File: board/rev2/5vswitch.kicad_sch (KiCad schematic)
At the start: 13 parts, among them Q1 WSD40120DN56G, U3 LM5050-1, U4 TPS259472ARPWR

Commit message: Board GPIO allocation
- and usbmux

still need to do termination on the big buses + a bunch of bypass caps
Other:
- company: (none) -> MLABS
- title: (none) -> 5V Multiplexer
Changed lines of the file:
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@@
 	(generator_version "9.0")
 	(paper "A4")
+	(title_block
+		(title "5V Multiplexer")
+		(rev "A")
+		(company "MLABS")
+		(comment 1 "MSign-NG")
+	)
 	(junction
 		(at 220.98 71.12)

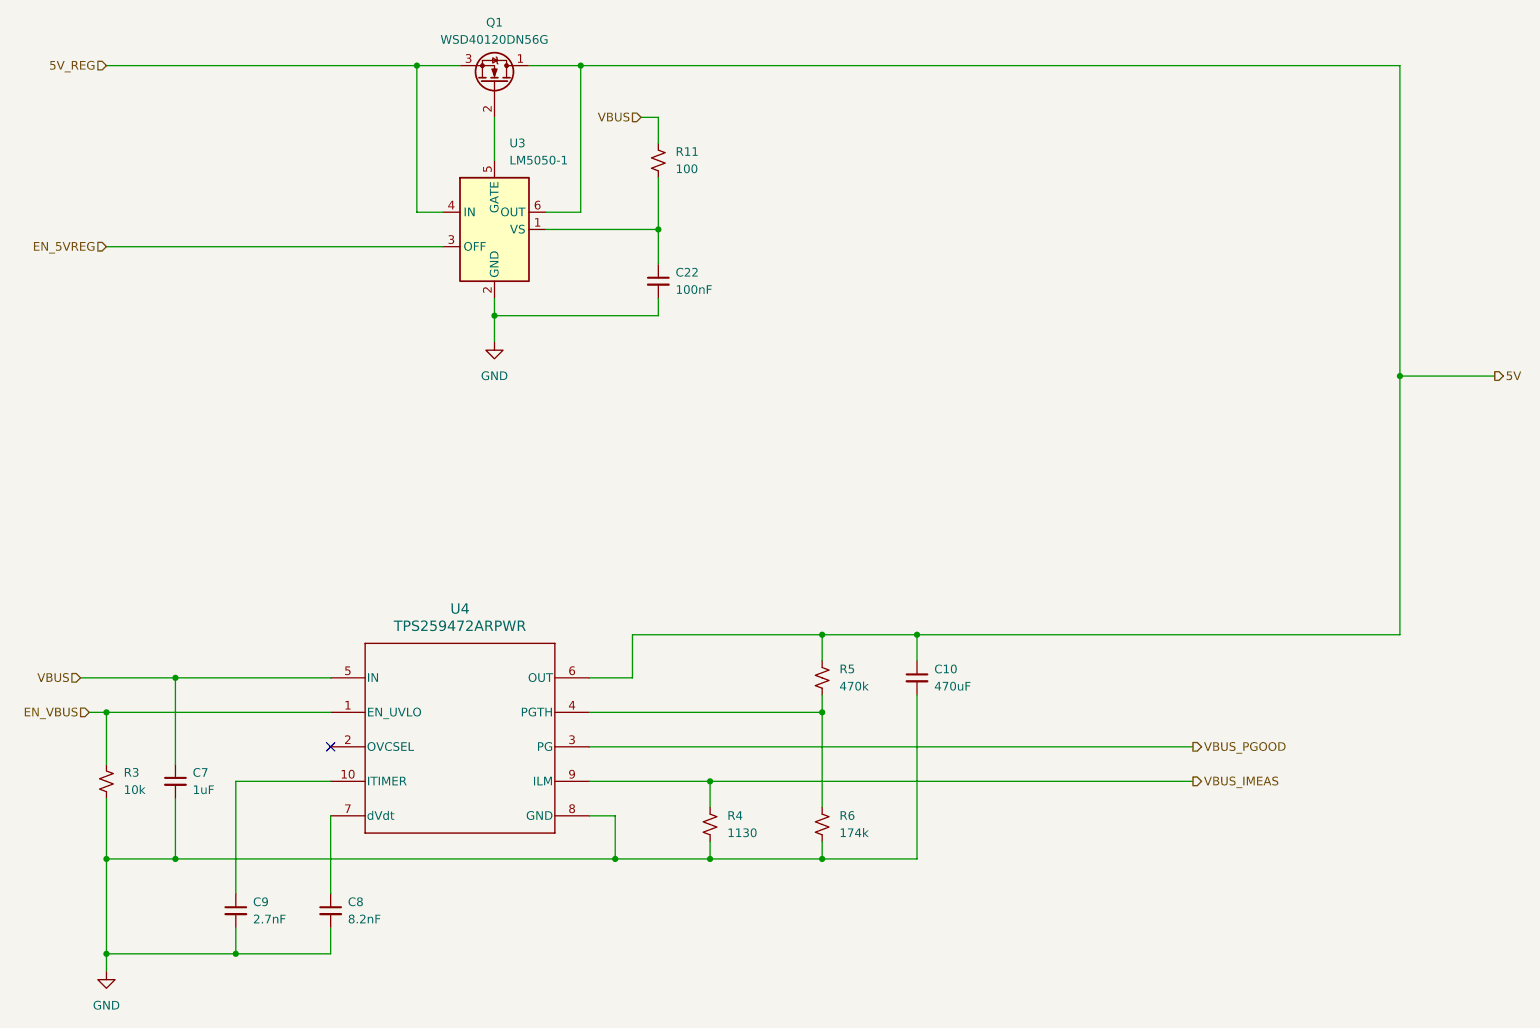
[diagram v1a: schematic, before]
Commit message: Continue board, assign caps/res, adjust for JLC availability
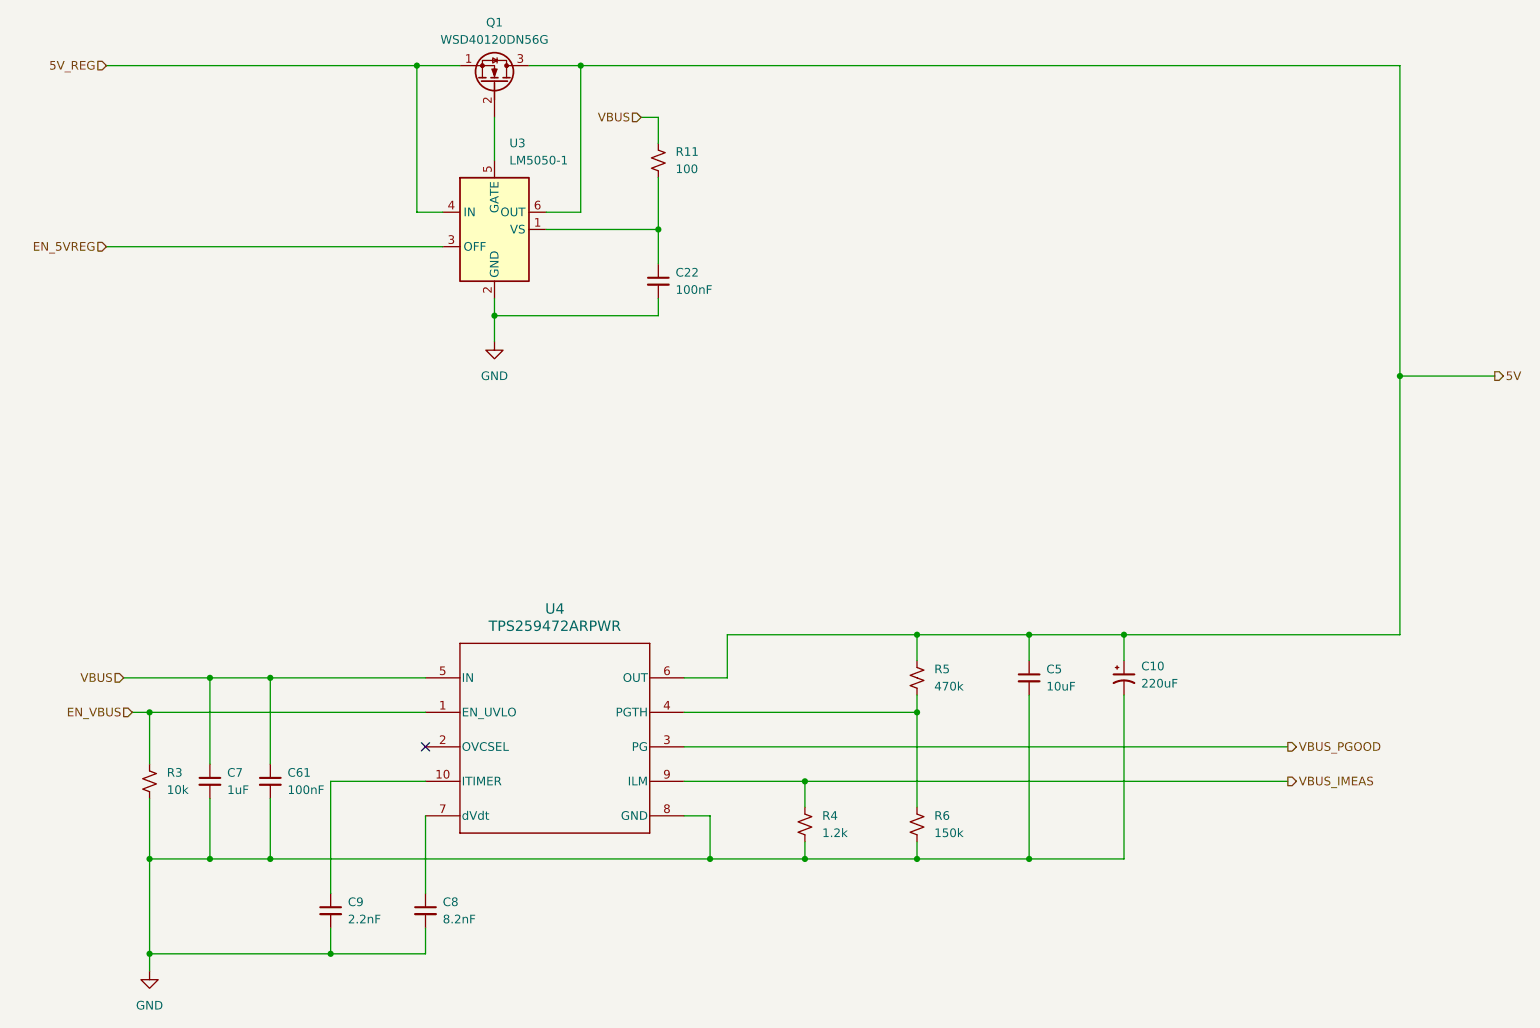
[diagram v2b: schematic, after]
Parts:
- added C5: 10uF, Capacitor_SMD:C_1210_3225Metric, symbol Device:C_Small
- added C61: 100nF, Capacitor_SMD:C_0402_1005Metric, symbol Device:C_Small
- C10: value 470uF -> 220uF; footprint (none) -> Capacitor_THT:CP_Radial_D8.0mm_P3.50mm; symbol Device:C_Small -> Device:C_Polarized_Small_US; Part (none) -> ERS1VM221F12OT
- C22: footprint (none) -> Capacitor_SMD:C_0402_1005Metric; Part (none) -> CL05B104KB54PNC
- C7: footprint (none) -> Capacitor_SMD:C_0603_1608Metric; Part (none) -> CL10A105KB8NNNC
- C8: footprint (none) -> Capacitor_SMD:C_0603_1608Metric; Part (none) -> 0603B822K500NT
- C9: value 2.7nF -> 2.2nF; footprint (none) -> Capacitor_SMD:C_0603_1608Metric; Part (none) -> 0603B222K500NT
- Q1: footprint (none) -> Transistor_FET_Winsok:DFN-8_L4.9-W6.0-P1.27-LS6.1-BL; symbol Device:Q_NMOS_DGS -> Transistor_FET:Q_NMOS_SGD
- R11: footprint (none) -> Resistor_SMD:R_1206_3216Metric; Part (none) -> 1206W4F1000T5E
- R3: footprint (none) -> Resistor_SMD:R_0805_2012Metric; Part (none) -> 0805W8F1002T5E
- R4: value 1130 -> 1.2k; footprint (none) -> Resistor_SMD:R_0805_2012Metric; Part (none) -> 0805W8F1201T5E
- R5: footprint (none) -> Resistor_SMD:R_0805_2012Metric; Part (none) -> 0805W8F4703T5E
- R6: value 174k -> 150k; footprint (none) -> Resistor_SMD:R_0805_2012Metric; Part (none) -> 0805W8F1503T5E
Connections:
- net 5V: now also Q1.3 (D), C5.1; no longer Q1.1 (D)
- net 5V_REG: now also Q1.1 (S); no longer Q1.3 (S)
- net GND: now also C5.2, C61.2
- net VBUS: now also C61.1
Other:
- moved on the sheet: C7, C8, C9, R3, R4, R5, R6, U4

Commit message: Start new PCB
- all footprints setup
- need to setup netclasses next, tho
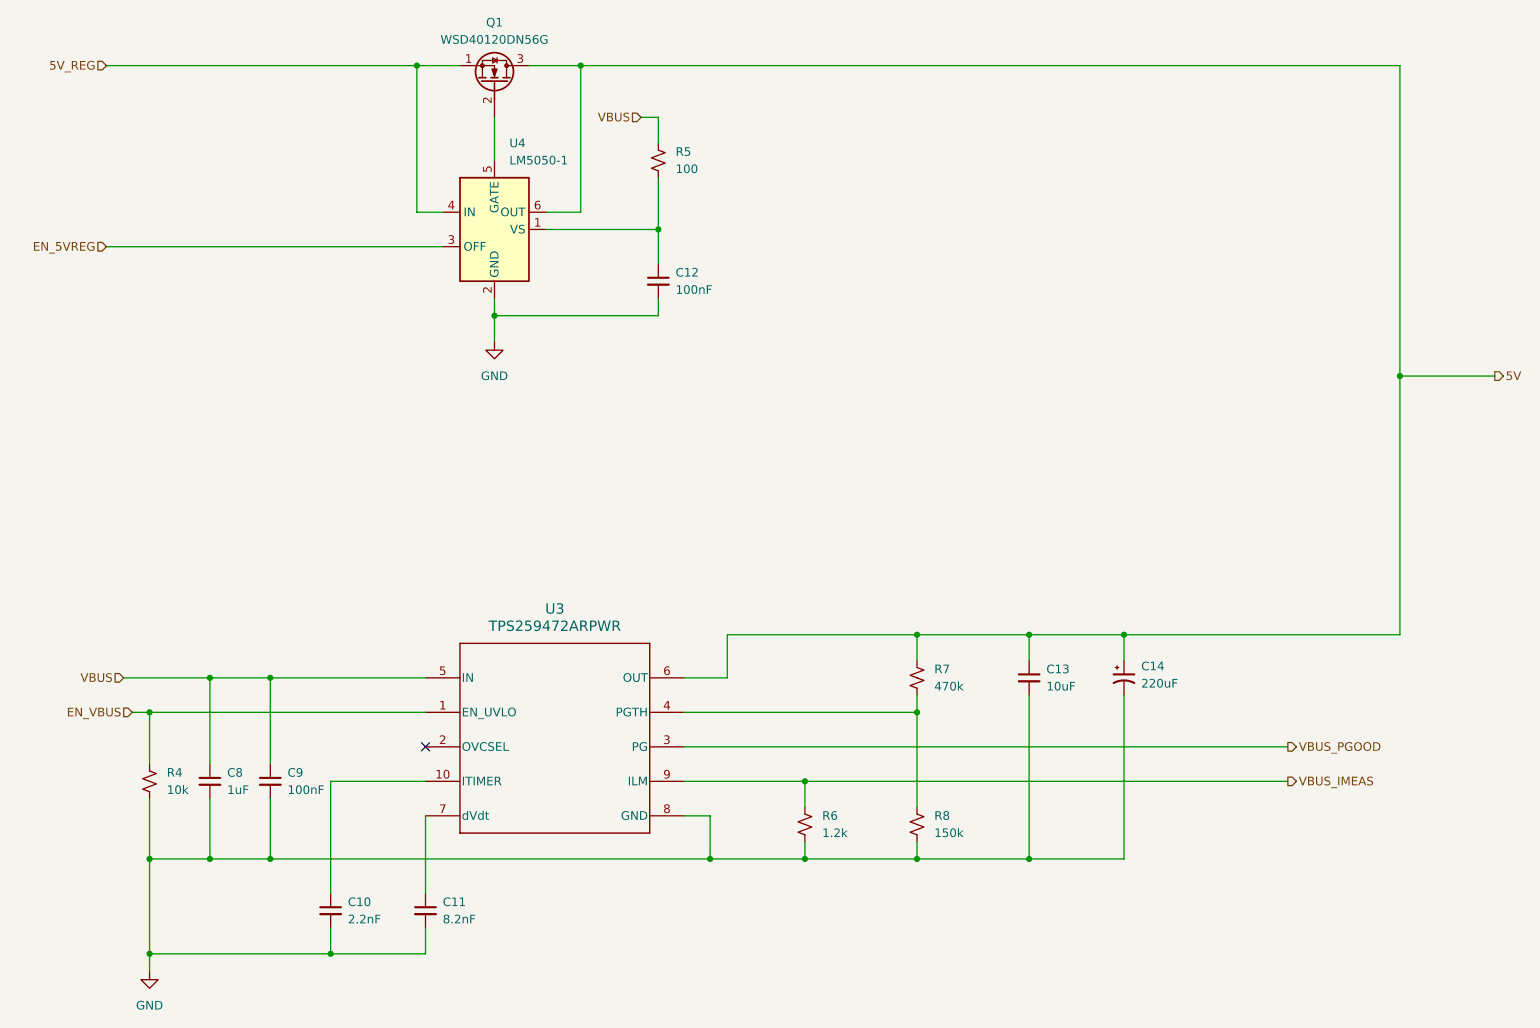
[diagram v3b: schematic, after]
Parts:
- Q1: Part (none) -> WSD40120DN56G
- U3: renamed from U4; footprint RPW0010A-MFG -> TI_EFuse:VQFN-10_L2.0-W2.0-P0.45-TL; Part (none) -> TPS259472ARPWR
- U4: renamed from U3; Part (none) -> LM5050-1
- renumbered C9 to C10, C8 to C11, C22 to C12, C5 to C13, C10 to C14, C7 to C8, C61 to C9, R3 to R4, R11 to R5, R4 to R6, R5 to R7, R6 to R8
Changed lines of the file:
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@@
 		(dnp no)
 		(fields_autoplaced yes)
-		(property "Reference" "C10"
+		(property "Reference" "C14"
 			(at 182.88 113.8681 0)
 			(effects
@@
 			(project "mainboard"
 				(path "/32eb05c7-b4a6-42f3-8fb3-43453631100f/802d77e5-f72d-443e-abfe-d20b44acef6c/65e76cbc-a8ae-47e0-859c-8ff07b1a8d6c"
-					(reference "C10")
+					(reference "C14")
 					(unit 1)
 				)
@@
 		(dnp no)
 		(fields_autoplaced yes)
-		(property "Reference" "C5"
+		(property "Reference" "C13"
 			(at 168.91 114.3062 0)
 			(effects
@@
 			(project "mainboard"
 				(path "/32eb05c7-b4a6-42f3-8fb3-43453631100f/802d77e5-f72d-443e-abfe-d20b44acef6c/65e76cbc-a8ae-47e0-859c-8ff07b1a8d6c"
-					(reference "C5")
+					(reference "C13")
 					(unit 1)
 				)
@@
 		(dnp no)
 		(fields_autoplaced yes)
-		(property "Reference" "C22"
+		(property "Reference" "C12"
 			(at 114.3 55.8862 0)
 			(effects
@@
 			(project ""
 				(path "/32eb05c7-b4a6-42f3-8fb3-43453631100f/802d77e5-f72d-443e-abfe-d20b44acef6c/65e76cbc-a8ae-47e0-859c-8ff07b1a8d6c"
-					(reference "C22")
+					(reference "C12")
 					(unit 1)
 				)
@@
 		(dnp no)
 		(fields_autoplaced yes)
-		(property "Reference" "U3"
+		(property "Reference" "U4"
 			(at 89.8241 36.83 0)
 			(effects
@@
 			)
 		)
+		(property "Part" "LM5050-1"
+			(at 87.63 49.53 0)
+			(effects
+				(font
+					(size 1.27 1.27)
+				)
+				(hide yes)
+			)
+		)
 		(pin "6"
 		)
@@
 			(project ""
 				(path "/32eb05c7-b4a6-42f3-8fb3-43453631100f/802d77e5-f72d-443e-abfe-d20b44acef6c/65e76cbc-a8ae-47e0-859c-8ff07b1a8d6c"
-					(reference "U3")
+					(reference "U4")
 					(unit 1)
 				)
@@
 		(dnp no)
 		(fields_autoplaced yes)
-		(property "Reference" "#PWR17"
+		(property "Reference" "#PWR08"
 			(at 87.63 72.39 0)
 			(effects
@@
 			(project ""
 				(path "/32eb05c7-b4a6-42f3-8fb3-43453631100f/802d77e5-f72d-443e-abfe-d20b44acef6c/65e76cbc-a8ae-47e0-859c-8ff07b1a8d6c"
-					(reference "#PWR17")
+					(reference "#PWR08")
 					(unit 1)
 				)
@@
 		(dnp no)
 		(fields_autoplaced yes)
-		(property "Reference" "R4"
+		(property "Reference" "R6"
 			(at 135.89 135.8899 0)
 			(effects
@@
 			(project "mainboard"
 				(path "/32eb05c7-b4a6-42f3-8fb3-43453631100f/802d77e5-f72d-443e-abfe-d20b44acef6c/65e76cbc-a8ae-47e0-859c-8ff07b1a8d6c"
-					(reference "R4")
+					(reference "R6")
 					(unit 1)
 				)
@@
 		(dnp no)
 		(fields_autoplaced yes)
-		(property "Reference" "R3"
+		(property "Reference" "R4"
 			(at 39.37 129.5399 0)
 			(effects
@@
 			(project "mainboard"
 				(path "/32eb05c7-b4a6-42f3-8fb3-43453631100f/802d77e5-f72d-443e-abfe-d20b44acef6c/65e76cbc-a8ae-47e0-859c-8ff07b1a8d6c"
-					(reference "R3")
+					(reference "R4")
 					(unit 1)
 				)
@@
 		(dnp no)
 		(fields_autoplaced yes)
-		(property "Reference" "#PWR09"
+		(property "Reference" "#PWR07"
 			(at 36.83 165.1 0)
 			(effects
@@
 			(project "mainboard"
 				(path "/32eb05c7-b4a6-42f3-8fb3-43453631100f/802d77e5-f72d-443e-abfe-d20b44acef6c/65e76cbc-a8ae-47e0-859c-8ff07b1a8d6c"
-					(reference "#PWR09")
+					(reference "#PWR07")
 					(unit 1)
 				)
@@
 		(dnp no)
 		(fields_autoplaced yes)
-		(property "Reference" "R11"
+		(property "Reference" "R5"
 			(at 114.3 38.0999 0)
 			(effects
@@
 			(project "mainboard"
 				(path "/32eb05c7-b4a6-42f3-8fb3-43453631100f/802d77e5-f72d-443e-abfe-d20b44acef6c/65e76cbc-a8ae-47e0-859c-8ff07b1a8d6c"
-					(reference "R11")
+					(reference "R5")
 					(unit 1)
 				)
@@
 		(dnp no)
 		(fields_autoplaced yes)
-		(property "Reference" "U4"
+		(property "Reference" "U3"
 			(at 96.52 105.41 0)
 			(effects
@@
 			)
 		)
-		(property "Footprint" "RPW0010A-MFG"
+		(property "Footprint" "TI_EFuse:VQFN-10_L2.0-W2.0-P0.45-TL"
 			(at 77.47 115.57 0)
 			(effects
@@
 			)
 		)
+		(property "Part" "TPS259472ARPWR"
+			(at 77.47 115.57 0)
+			(effects
+				(font
+					(size 1.27 1.27)
+				)
+				(hide yes)
+			)
+		)
 		(pin "9"
 		)
@@
 			(project "mainboard"
 				(path "/32eb05c7-b4a6-42f3-8fb3-43453631100f/802d77e5-f72d-443e-abfe-d20b44acef6c/65e76cbc-a8ae-47e0-859c-8ff07b1a8d6c"
-					(reference "U4")
+					(reference "U3")
 					(unit 1)
 				)
@@
 		(dnp no)
 		(fields_autoplaced yes)
-		(property "Reference" "C7"
+		(property "Reference" "C8"
 			(at 48.26 129.5462 0)
 			(effects
@@
 			(project "mainboard"
 				(path "/32eb05c7-b4a6-42f3-8fb3-43453631100f/802d77e5-f72d-443e-abfe-d20b44acef6c/65e76cbc-a8ae-47e0-859c-8ff07b1a8d6c"
-					(reference "C7")
+					(reference "C8")
 					(unit 1)
 				)
@@
 		(dnp no)
 		(fields_autoplaced yes)
-		(property "Reference" "C61"
+		(property "Reference" "C9"
 			(at 57.15 129.5462 0)
 			(effects
@@
 			(project "mainboard"
 				(path "/32eb05c7-b4a6-42f3-8fb3-43453631100f/802d77e5-f72d-443e-abfe-d20b44acef6c/65e76cbc-a8ae-47e0-859c-8ff07b1a8d6c"
-					(reference "C61")
+					(reference "C9")
 					(unit 1)
 				)
@@
 		(dnp no)
 		(fields_autoplaced yes)
-		(property "Reference" "C8"
+		(property "Reference" "C11"
 			(at 80.01 148.5962 0)
 			(effects
@@
 			(project "mainboard"
 				(path "/32eb05c7-b4a6-42f3-8fb3-43453631100f/802d77e5-f72d-443e-abfe-d20b44acef6c/65e76cbc-a8ae-47e0-859c-8ff07b1a8d6c"
-					(reference "C8")
+					(reference "C11")
 					(unit 1)
 				)
@@
 		(dnp no)
 		(fields_autoplaced yes)
-		(property "Reference" "C9"
+		(property "Reference" "C10"
 			(at 66.04 148.5962 0)
 			(effects
@@
 			(project "mainboard"
 				(path "/32eb05c7-b4a6-42f3-8fb3-43453631100f/802d77e5-f72d-443e-abfe-d20b44acef6c/65e76cbc-a8ae-47e0-859c-8ff07b1a8d6c"
-					(reference "C9")
+					(reference "C10")
 					(unit 1)
 				)
@@
 			)
 		)
+		(property "Part" "WSD40120DN56G"
+			(at 87.63 27.94 90)
+			(effects
+				(font
+					(size 1.27 1.27)
+				)
+				(hide yes)
+			)
+		)
 		(pin "1"
 		)
@@
 		(dnp no)
 		(fields_autoplaced yes)
-		(property "Reference" "R6"
+		(property "Reference" "R8"
 			(at 152.4 135.8899 0)
 			(effects
@@
 			(project "mainboard"
 				(path "/32eb05c7-b4a6-42f3-8fb3-43453631100f/802d77e5-f72d-443e-abfe-d20b44acef6c/65e76cbc-a8ae-47e0-859c-8ff07b1a8d6c"
-					(reference "R6")
+					(reference "R8")
 					(unit 1)
 				)
@@
 		(dnp no)
 		(fields_autoplaced yes)
-		(property "Reference" "R5"
+		(property "Reference" "R7"
 			(at 152.4 114.2999 0)
 			(effects
@@
 			(project "mainboard"
 				(path "/32eb05c7-b4a6-42f3-8fb3-43453631100f/802d77e5-f72d-443e-abfe-d20b44acef6c/65e76cbc-a8ae-47e0-859c-8ff07b1a8d6c"
-					(reference "R5")
-					(unit 1)
-				)
+					(reference "R7")
+					(unit 1)
+				)

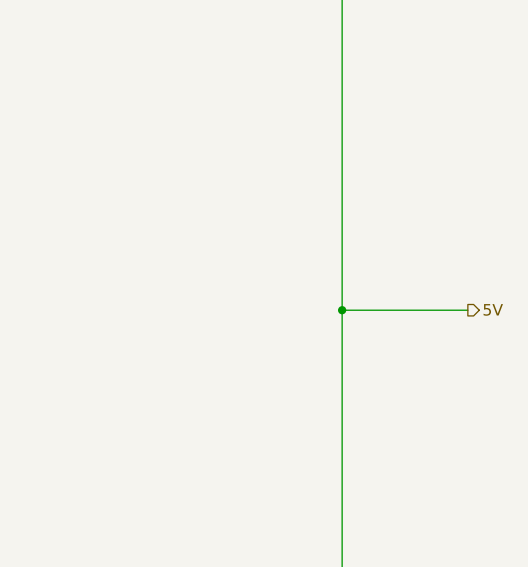
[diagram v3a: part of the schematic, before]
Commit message: Add netclasses, more footprints, fix ERC
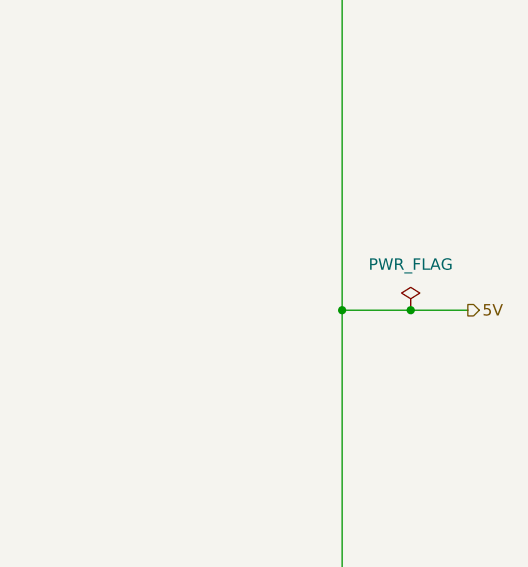
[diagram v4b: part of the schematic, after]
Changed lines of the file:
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@@
+	)
+	(junction
+		(at 228.6 71.12)
+		(diameter 0)
+		(color 0 0 0 0)
 	)
 	(junction
@@
 	(wire
 		(pts
+			(xy 228.6 71.12) (xy 234.95 71.12)
+		)
+		(stroke
+			(width 0)
+			(type default)
+		)
+	)
+	(wire
+		(pts
 			(xy 36.83 120.65) (xy 77.47 120.65)
 		)
@@
 	(wire
 		(pts
-			(xy 220.98 71.12) (xy 234.95 71.12)
+			(xy 220.98 71.12) (xy 228.6 71.12)
 		)
 		(stroke
@@
 					(unit 1)
 				)
+			)
+		)
+	)
+	(symbol
+		(lib_id "power:PWR_FLAG")
+		(at 228.6 71.12 0)
+		(unit 1)
+		(exclude_from_sim no)
+		(in_bom yes)
+		(on_board yes)
+		(dnp no)
+		(fields_autoplaced yes)
+		(property "Reference" "#FLG01"
+			(at 228.6 69.215 0)
+			(effects
+				(font
+					(size 1.27 1.27)
+				)
+				(hide yes)
+			)
+		)
+		(property "Value" "PWR_FLAG"
+			(at 228.6 66.04 0)
+			(effects
+				(font
+					(size 1.27 1.27)
+				)
+			)
+		)
+		(property "Footprint" ""
+			(at 228.6 71.12 0)
+			(effects
+				(font
+					(size 1.27 1.27)
+				)
+				(hide yes)
+			)
+		)
+		(property "Datasheet" "~"
+			(at 228.6 71.12 0)
+			(effects
+				(font
+					(size 1.27 1.27)
+				)
+				(hide yes)
+			)
+		)
+		(property "Description" "Special symbol for telling ERC where power comes from"
+			(at 228.6 71.12 0)
+			(effects
+				(font
+					(size 1.27 1.27)
+				)
+				(hide yes)
+			)
+		)
+		(pin "1"
+		)
+		(instances
+			(project ""
+				(path "/32eb05c7-b4a6-42f3-8fb3-43453631100f/802d77e5-f72d-443e-abfe-d20b44acef6c/65e76cbc-a8ae-47e0-859c-8ff07b1a8d6c"
+					(reference "#FLG01")
+					(unit 1)
+				)
